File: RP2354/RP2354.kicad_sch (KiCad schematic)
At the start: 38 parts, among them J1 USB_C_Receptacle_USB2.0_14P, J2 SWD, J3 Conn_01x12_Pin, J4 Conn_01x12_Pin, U1 TCR8BM33A_L3F, U14 RP2354A, Y1 Crystal

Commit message: Quick pass at ERC
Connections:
- no-connect marks 7 -> 12
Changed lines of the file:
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@@
 	)
 	(junction
+		(at 191.77 53.34)
+		(diameter 0)
+		(color 0 0 0 0)
+	)
+	(junction
 		(at 195.58 6.35)
 		(diameter 0)
@@
 	)
 	(junction
+		(at 130.81 33.02)
+		(diameter 0)
+		(color 0 0 0 0)
+	)
+	(junction
 		(at 114.3 140.97)
 		(diameter 0)
@@
 	)
 	(no_connect
+		(at 138.43 100.33)
+	)
+	(no_connect
 		(at 30.48 91.44)
 	)
 	(no_connect
+		(at 138.43 92.71)
+	)
+	(no_connect
+		(at 138.43 97.79)
+	)
+	(no_connect
 		(at 87.63 87.63)
 	)
@@
 	)
 	(no_connect
+		(at 138.43 95.25)
+	)
+	(no_connect
+		(at 138.43 90.17)
+	)
+	(no_connect
 		(at 87.63 92.71)
 	)
@@
 	(wire
 		(pts
-			(xy 130.81 6.35) (xy 132.08 6.35)
-		)
-		(stroke
-			(width 0)
-			(type default)
-		)
-	)
-	(wire
-		(pts
 			(xy 71.12 62.23) (xy 87.63 62.23)
 		)
@@
 	)
 	(symbol
+		(lib_id "power:PWR_FLAG")
+		(at 77.47 25.4 0)
+		(unit 1)
+		(exclude_from_sim no)
+		(in_bom yes)
+		(on_board yes)
+		(dnp no)
+		(fields_autoplaced yes)
+		(property "Reference" "#FLG03"
+			(at 77.47 23.495 0)
+			(effects
+				(font
+					(size 1.27 1.27)
+				)
+				(hide yes)
+			)
+		)
+		(property "Value" "PWR_FLAG"
+			(at 77.47 20.32 0)
+			(effects
+				(font
+					(size 1.27 1.27)
+				)
+			)
+		)
+		(property "Footprint" ""
+			(at 77.47 25.4 0)
+			(effects
+				(font
+					(size 1.27 1.27)
+				)
+				(hide yes)
+			)
+		)
+		(property "Datasheet" "~"
+			(at 77.47 25.4 0)
+			(effects
+				(font
+					(size 1.27 1.27)
+				)
+				(hide yes)
+			)
+		)
+		(property "Description" "Special symbol for telling ERC where power comes from"
+			(at 77.47 25.4 0)
+			(effects
+				(font
+					(size 1.27 1.27)
+				)
+				(hide yes)
+			)
+		)
+		(pin "1"
+		)
+		(instances
+			(project "RP2354"
+				(path "/75796f0e-c7bb-4022-b2fb-227ab57b0aaa"
+					(reference "#FLG03")
+					(unit 1)
+				)
+			)
+		)
+	)
+	(symbol
 		(lib_id "power:+1V1")
 		(at 64.77 25.4 0)
@@
 	)
 	(symbol
+		(lib_id "power:PWR_FLAG")
+		(at 191.77 53.34 0)
+		(unit 1)
+		(exclude_from_sim no)
+		(in_bom yes)
+		(on_board yes)
+		(dnp no)
+		(fields_autoplaced yes)
+		(property "Reference" "#FLG01"
+			(at 191.77 51.435 0)
+			(effects
+				(font
+					(size 1.27 1.27)
+				)
+				(hide yes)
+			)
+		)
+		(property "Value" "PWR_FLAG"
+			(at 191.77 48.26 0)
+			(effects
+				(font
+					(size 1.27 1.27)
+				)
+			)
+		)
+		(property "Footprint" ""
+			(at 191.77 53.34 0)
+			(effects
+				(font
+					(size 1.27 1.27)
+				)
+				(hide yes)
+			)
+		)
+		(property "Datasheet" "~"
+			(at 191.77 53.34 0)
+			(effects
+				(font
+					(size 1.27 1.27)
+				)
+				(hide yes)
+			)
+		)
+		(property "Description" "Special symbol for telling ERC where power comes from"
+			(at 191.77 53.34 0)
+			(effects
+				(font
+					(size 1.27 1.27)
+				)
+				(hide yes)
+			)
+		)
+		(pin "1"
+		)
+		(instances
+			(project ""
+				(path "/75796f0e-c7bb-4022-b2fb-227ab57b0aaa"
+					(reference "#FLG01")
+					(unit 1)
+				)
+			)
+		)
+	)
+	(symbol
 		(lib_id "Device:C")
 		(at 64.77 33.02 0)
@@
 					(unit 1)
 				)
+			)
+		)
+	)
+	(symbol
+		(lib_id "power:PWR_FLAG")
+		(at 130.81 33.02 0)
+		(unit 1)
+		(exclude_from_sim no)
+		(in_bom yes)
+		(on_board yes)
+		(dnp no)
+		(fields_autoplaced yes)
+		(property "Reference" "#FLG02"
+			(at 130.81 31.115 0)
+			(effects
+				(font
+					(size 1.27 1.27)
+				)
+				(hide yes)
+			)
+		)
+		(property "Value" "PWR_FLAG"
+			(at 130.81 27.94 0)
+			(effects
+				(font
+					(size 1.27 1.27)
+				)
+			)
+		)
+		(property "Footprint" ""
+			(at 130.81 33.02 0)
+			(effects
+				(font
+					(size 1.27 1.27)
+				)
+				(hide yes)
+			)
+		)
+		(property "Datasheet" "~"
+			(at 130.81 33.02 0)
+			(effects
+				(font
+					(size 1.27 1.27)
+				)
+				(hide yes)
+			)
+		)
+		(property "Description" "Special symbol for telling ERC where power comes from"
+			(at 130.81 33.02 0)
+			(effects
+				(font
+					(size 1.27 1.27)
+				)
+				(hide yes)
+			)
+		)
+		(pin "1"
+		)
+		(instances
+			(project "RP2354"
+				(path "/75796f0e-c7bb-4022-b2fb-227ab57b0aaa"
+					(reference "#FLG02")
+					(unit 1)
+				)

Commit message: MPN's added for most parts. iBom export
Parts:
- C5: MFGR (none) -> Samsung; MPN (none) -> CL10C100JB8NFNC
- C6: MFGR TDK -> Samsung; MPN C1608C0G1H080D080AA -> CL10C100JB8NFNC
- D1: MFGR (none) -> Adafruit (10-pack!); MPN (none) -> 3341
- J1: MPN (none) -> TYPE-C-31-M-14
- RESET1, USBDEV1: MFGR (none) -> C&K; MPN (none) -> KMR241G LFS
- U1: MFGR (none) -> Toshiba Semiconductor and Storage; MPN (none) -> TCR8BM33A,L3F
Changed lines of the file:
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@@
+			)
+		)
+		(property "MFGR" "Adafruit (10-pack!)"
+			(at 38.1 91.44 0)
+			(effects
+				(font
+					(size 1.27 1.27)
+				)
+				(hide yes)
+			)
+		)
+		(property "MPN" "3341"
+			(at 38.1 91.44 0)
+			(effects
+				(font
+					(size 1.27 1.27)
+				)
+				(hide yes)
 			)
 		)
@@
 			)
 		)
+		(property "MFGR" "Toshiba Semiconductor and Storage"
+			(at 176.53 35.56 0)
+			(effects
+				(font
+					(size 1.27 1.27)
+				)
+				(hide yes)
+			)
+		)
+		(property "MPN" "TCR8BM33A,L3F"
+			(at 176.53 35.56 0)
+			(effects
+				(font
+					(size 1.27 1.27)
+				)
+				(hide yes)
+			)
+		)
 		(pin "4"
 		)
@@
 			)
 		)
+		(property "MFGR" "C&K"
+			(at 151.13 69.85 0)
+			(effects
+				(font
+					(size 1.27 1.27)
+				)
+				(hide yes)
+			)
+		)
+		(property "MPN" "KMR241G LFS"
+			(at 151.13 69.85 0)
+			(effects
+				(font
+					(size 1.27 1.27)
+				)
+				(hide yes)
+			)
+		)
 		(pin "1"
 		)
@@
 			)
 		)
-		(property "MFGR" ""
+		(property "MFGR" "Samsung"
 			(at 167.64 113.03 0)
 			(effects
@@
 			)
 		)
-		(property "MPN" ""
+		(property "MPN" "CL10C100JB8NFNC"
 			(at 167.64 113.03 0)
 			(effects
@@
 			)
 		)
-		(property "MFGR" ""
+		(property "MFGR" "C&K"
 			(at 151.13 87.63 0)
 			(effects
@@
 			)
 		)
-		(property "MPN" ""
+		(property "MPN" "KMR241G LFS"
 			(at 151.13 87.63 0)
 			(effects
@@
 			)
 		)
+		(property "MFGR" ""
+			(at 207.01 77.47 0)
+			(effects
+				(font
+					(size 1.27 1.27)
+				)
+				(hide yes)
+			)
+		)
+		(property "MPN" "TYPE-C-31-M-14"
+			(at 207.01 77.47 0)
+			(effects
+				(font
+					(size 1.27 1.27)
+				)
+				(hide yes)
+			)
+		)
 		(pin "A1"
 		)
@@
 			)
 		)
-		(property "MFGR" "TDK"
+		(property "MFGR" "Samsung"
 			(at 167.64 118.11 0)
 			(effects
@@
 			)
 		)
-		(property "MPN" "C1608C0G1H080D080AA"
+		(property "MPN" "CL10C100JB8NFNC"
 			(at 167.64 118.11 0)
 			(effects

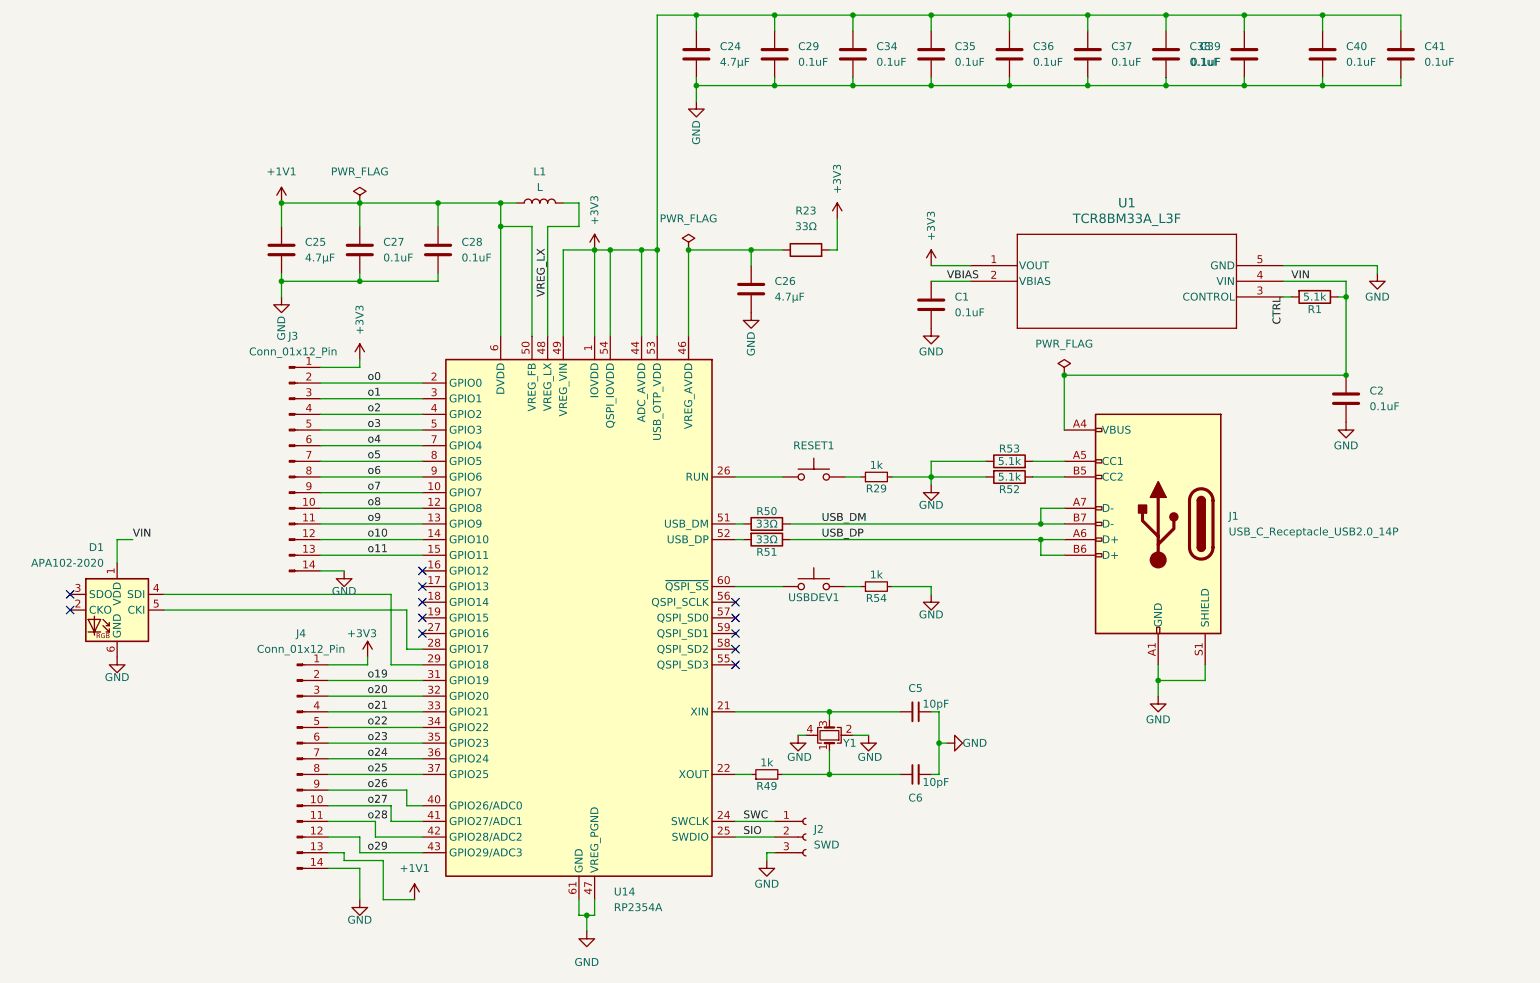
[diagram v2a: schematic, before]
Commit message: Updated with a larger 3.3V regulator. The added pins break out +5V/USB and IO12 as well. The TCR8BM is just too fiddly for DIY boards and the datasheet isn't good enough.
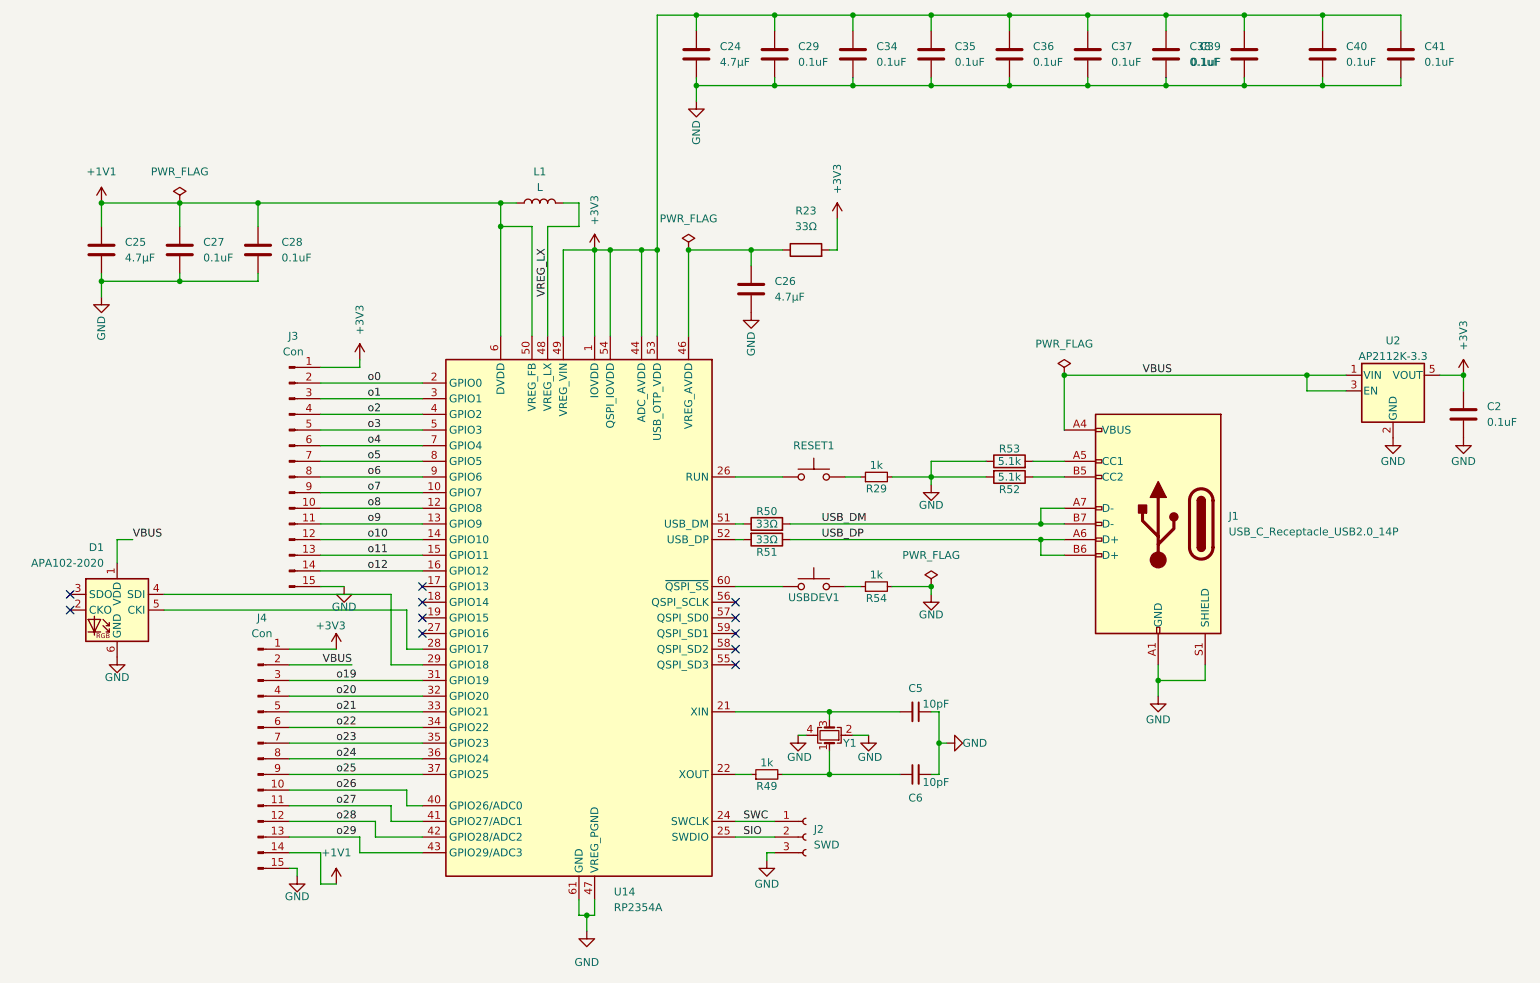
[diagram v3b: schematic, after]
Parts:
- removed C1: 0.1uF, Capacitor_SMD:C_0402_1005Metric, symbol Device:C
- removed R1: 5.1k, Resistor_SMD:R_0402_1005Metric, symbol Device:R
- removed U1: TCR8BM33A_L3F, DFN5B_TOS, symbol 2026-02-17_20-55-50:TCR8BM33A_L3F
- added U2: AP2112K-3.3, Package_TO_SOT_SMD:SOT-23-5, symbol Regulator_Linear:AP2112K-3.3
- J3, J4: value Conn_01x12_Pin -> Con; footprint Connector_PinHeader_2.54mm:PinHeader_1x14_P2.54mm_Vertical -> Connector_PinHeader_2.54mm:PinHeader_1x15_P2.54mm_Vertical; symbol Connector:Conn_01x14_Pin -> Connector:Conn_01x15_Pin
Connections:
- net +1V1: now also J4.14 (Pin_14); no longer J4.13 (Pin_13)
- net +3V3: now also C2.2, U2.5 (VOUT)
- net GND: now also J3.15 (Pin_15), J4.15 (Pin_15), U2.2 (GND); no longer J3.14 (Pin_14), J4.14 (Pin_14)
- net o19: now also J4.3 (Pin_3); no longer J4.2 (Pin_2)
- net o20: now also J4.4 (Pin_4); no longer J4.3 (Pin_3)
- net o21: now also J4.5 (Pin_5); no longer J4.4 (Pin_4)
- net o22: now also J4.6 (Pin_6); no longer J4.5 (Pin_5)
- net o23: now also J4.7 (Pin_7); no longer J4.6 (Pin_6)
- net o24: now also J4.8 (Pin_8); no longer J4.7 (Pin_7)
- net o25: now also J4.9 (Pin_9); no longer J4.8 (Pin_8)
- net o26: now also J4.10 (Pin_10); no longer J4.9 (Pin_9)
- net o27: now also J4.11 (Pin_11); no longer J4.10 (Pin_10)
- net o28: now also J4.12 (Pin_12); no longer J4.11 (Pin_11)
- net o29: now also J4.13 (Pin_13); no longer J4.12 (Pin_12)
- net o12: now reaches U14.16 (GPIO12)
- net o12: now also J3.14 (Pin_14)
- net VIN renamed VBUS
- net VBUS: now also J4.2 (Pin_2), U2.1 (VIN), U2.3 (EN); no longer C2.2
- no-connect marks 12 -> 11
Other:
- moved on the sheet: C2, C25, C27, C28

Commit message: Swapped for larger inductor footprint on L1. 0805 resistor is correct.
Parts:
- L1: footprint Inductor_SMD:L_0805_2012Metric -> Resistor_SMD:R_0805_2012Metric
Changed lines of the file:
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@@
 			)
 		)
-		(property "Footprint" "Inductor_SMD:L_0805_2012Metric"
+		(property "Footprint" "Resistor_SMD:R_0805_2012Metric"
 			(at 106.68 25.4 0)
 			(effects
